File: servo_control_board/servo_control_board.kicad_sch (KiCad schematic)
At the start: 18 parts, among them J1 Conn_01x03_Pin, J2 Conn_01x03_Pin, J3 Conn_01x03_Pin, J4 Conn_01x03_Pin, J5 Conn_01x03_Pin, J6 Conn_01x03_Pin, J7 Conn_01x02_Pin, J8 Conn_01x02_Socket, U1 LTV-846

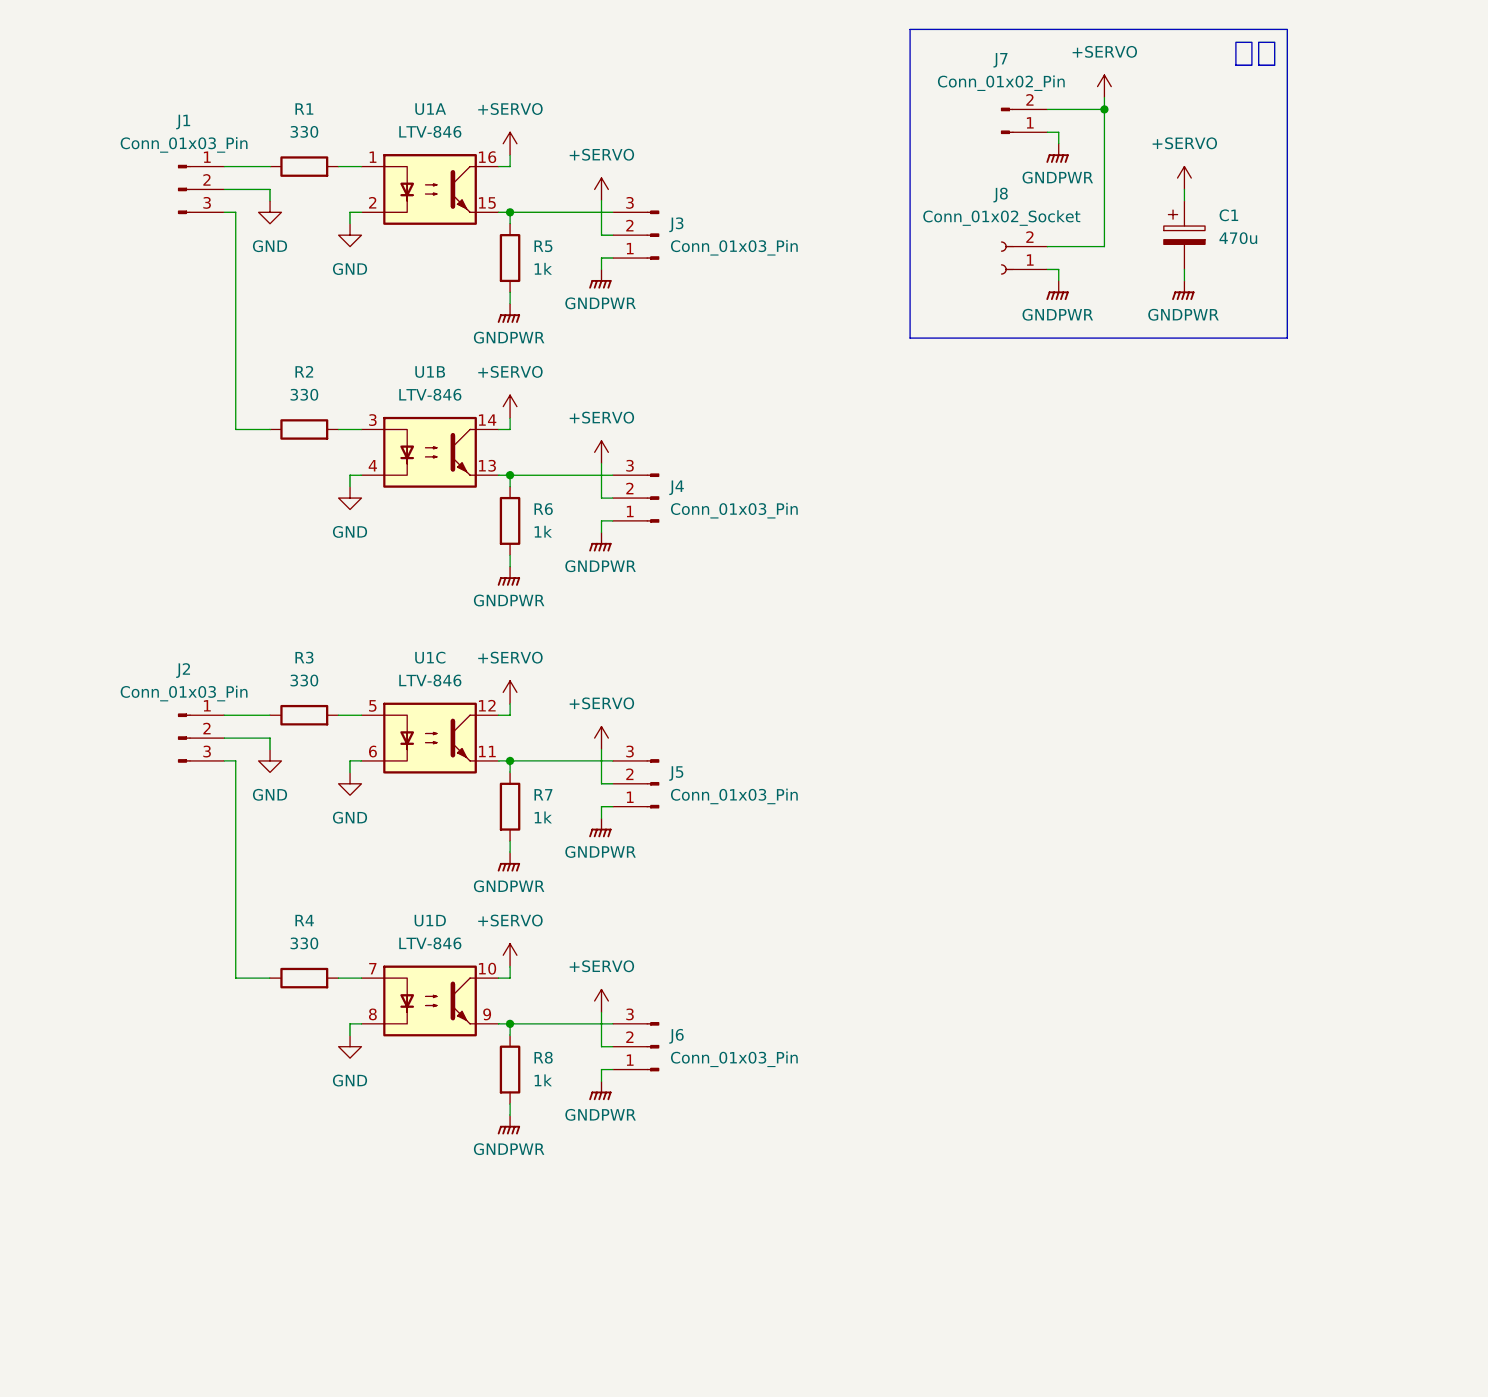
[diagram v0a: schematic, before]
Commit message: サーボ制御基板　使用するフォトカプラを変更 もともと使っていたLTV-846には以下のような問題点があったため． ・応答速度が遅く，サーボの角度にズレが生じる恐れがある ・応答速度を上げようと電流値を上げると，GPIOへの要求電流上昇やCTR不足が生じる
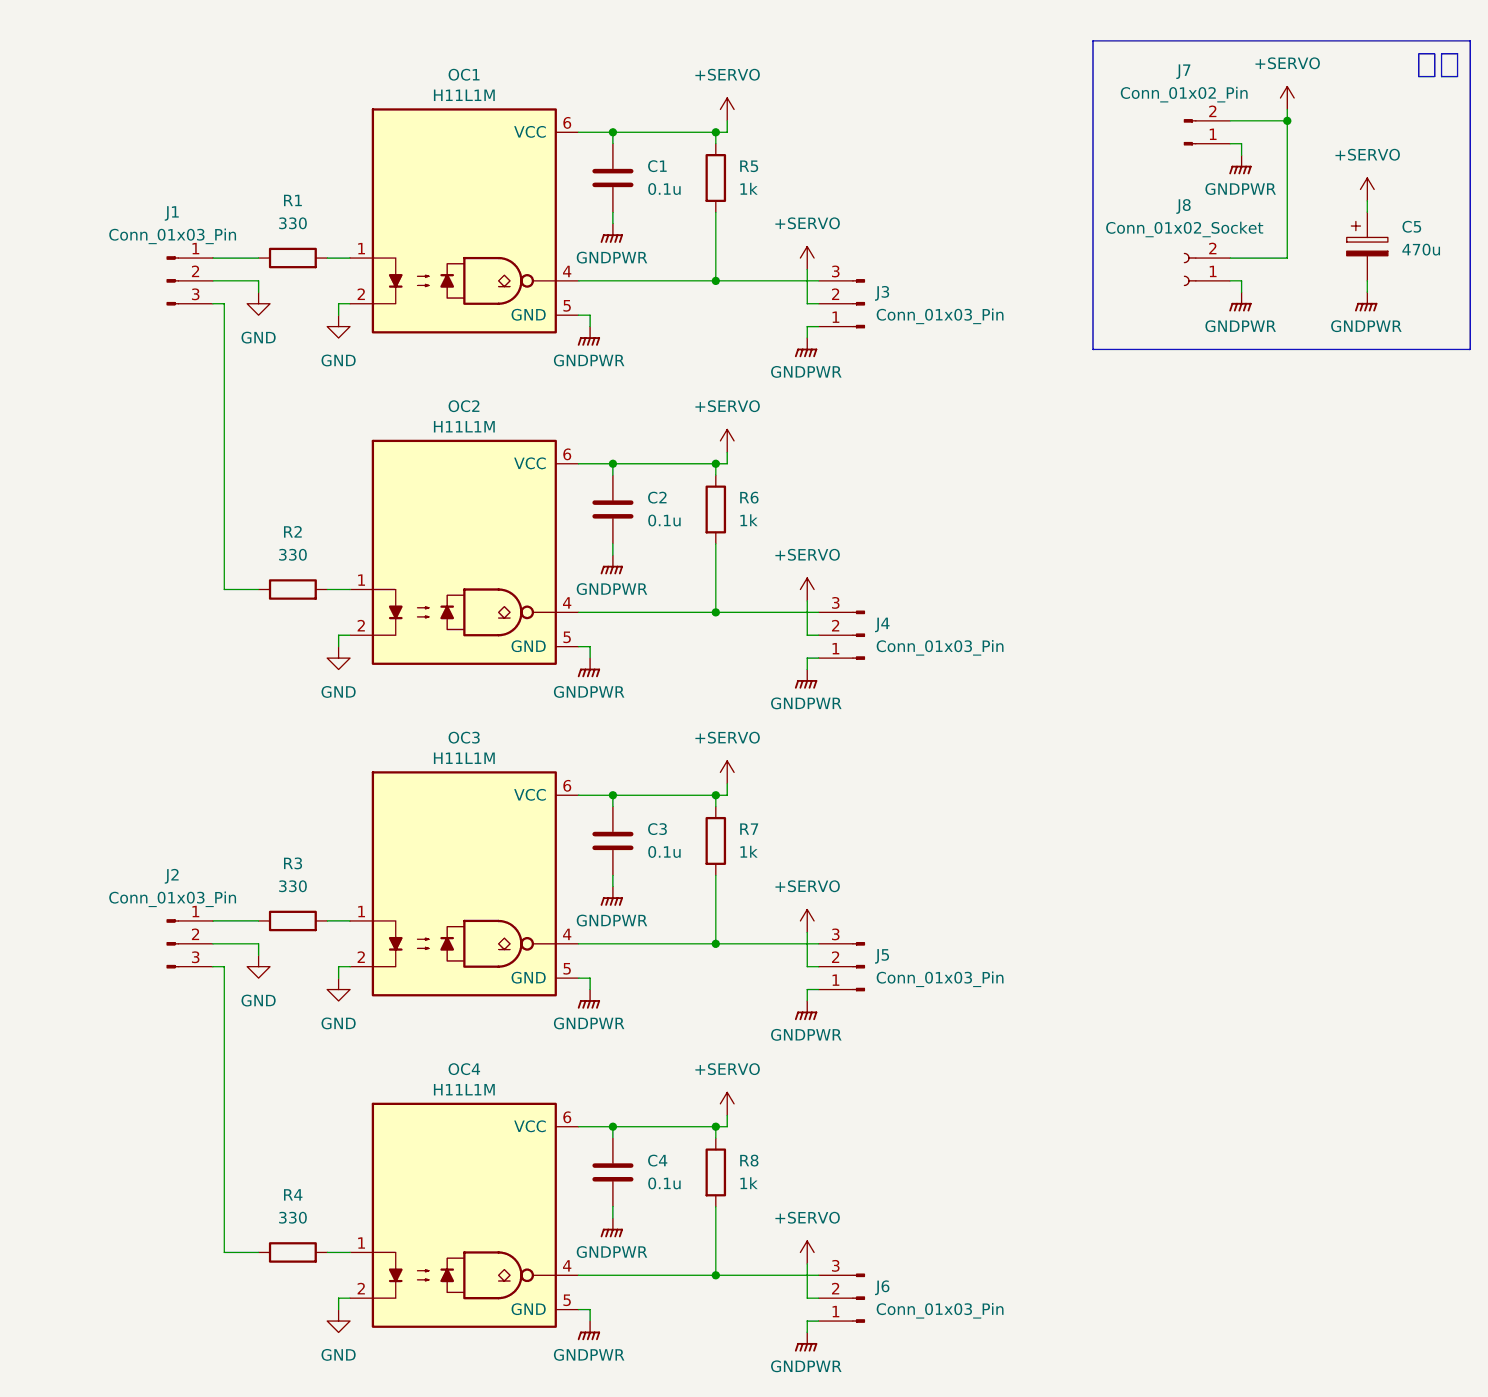
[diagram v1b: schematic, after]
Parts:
- removed U1: LTV-846, Package_DIP:DIP-16_W7.62mm, symbol Isolator:LTV-847
- added C1, C2, C3, C4: 0.1u, PCM_Package_DIP_AKL:DIP-6_W7.62mm_LongPads, symbol Device:C
- added OC1, OC2, OC3, OC4: H11L1M, PCM_Package_DIP_AKL:DIP-6_W7.62mm_LongPads, symbol PCM_Optocoupler_Logic_AKL:H11L1M
- J1, J2: footprint Package_DIP:DIP-16_W7.62mm -> OU_connector:DF1E-3P-2.5DS
- J3, J4, J5, J6: footprint Package_SO:TSSOP-16_4.4x5mm_P0.65mm -> Connector_PinHeader_2.54mm:PinHeader_1x03_P2.54mm_Vertical
- J7: footprint (none) -> OU_connector:AMASS_XT30PW-M_1x02_P2.50mm_Horizontal
- J8: footprint (none) -> OU_connector:AMASS_XT30PW-F_1x02_P2.50mm_Horizontal
- renumbered C1 to C5
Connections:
- net +SERVO: now also R5.1, R6.1, R7.1, R8.1, C1.2, C2.2, C3.2, C4.2, OC1.6 (VCC), OC2.6 (VCC), OC3.6 (VCC), OC4.6 (VCC)
- net GND: now also OC1.2, OC2.2, OC3.2, OC4.2
- net GNDPWR: now also C1.1, C2.1, C3.1, C4.1, OC1.5 (GND), OC2.5 (GND), OC3.5 (GND), OC4.5 (GND); no longer R5.2, R6.2, R7.2, R8.2
- net at J6.3 (Pin_3): now also R8.2, OC4.4; no longer R8.1
- net at J3.3 (Pin_3): now also R5.2, OC1.4; no longer R5.1
- net at J5.3 (Pin_3): now also R7.2, OC3.4; no longer R7.1
- net at R3.2: now also OC3.1
- net at J4.3 (Pin_3): now also R6.2, OC2.4; no longer R6.1
- net at R1.2: now also OC1.1
- net at R4.2: now also OC4.1
- net at R2.2: now also OC2.1
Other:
- moved on the sheet: C5, J1, J2, J3, J7, J8, R1, R2, R3, R4

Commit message: サーボ制御基板　フットプリント割当まで完了
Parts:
- C1, C2, C3, C4: footprint PCM_Package_DIP_AKL:DIP-6_W7.62mm_LongPads -> Capacitor_THT:C_Disc_D5.0mm_W2.5mm_P2.50mm; Buy_URL (none) -> https://akizukidenshi.com/catalog/g/g113582/
- J3, J4, J5, J6: Buy_URL (none) -> https://akizukidenshi.com/catalog/g/g100167/
- J7: Buy_URL (none) -> https://akizukidenshi.com/catalog/g/g117949/
- J8: Buy_URL (none) -> https://akizukidenshi.com/catalog/g/g117948/
- OC1, OC2, OC3, OC4: Buy_URL (none) -> https://akizukidenshi.com/catalog/g/g131184/
- R1, R2, R3, R4: footprint (none) -> Resistor_THT:R_Axial_DIN0207_L6.3mm_D2.5mm_P2.54mm_Vertical; Buy_URL (none) -> https://akizukidenshi.com/catalog/g/g125331/
- R5, R6, R7, R8: footprint (none) -> Resistor_THT:R_Axial_DIN0207_L6.3mm_D2.5mm_P2.54mm_Vertical; Buy_URL (none) -> https://akizukidenshi.com/catalog/g/g125102/

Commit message: サーボ制御基板　ピンヘッダのフットプリントを変更
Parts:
- J3, J4, J5, J6: footprint Connector_PinHeader_2.54mm:PinHeader_1x03_P2.54mm_Vertical -> Connector_PinHeader_2.54mm:PinHeader_1x03_P2.54mm_Horizontal; Buy_URL https://akizukidenshi.com/catalog/g/g100167/ -> https://akizukidenshi.com/catalog/g/g101627/
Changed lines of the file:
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@@
 			)
 		)
-		(property "Footprint" "Connector_PinHeader_2.54mm:PinHeader_1x03_P2.54mm_Vertical"
+		(property "Footprint" "Connector_PinHeader_2.54mm:PinHeader_1x03_P2.54mm_Horizontal"
 			(at 106.68 121.92 0)
 			(hide yes)
@@
 			)
 		)
-		(property "Buy_URL" "https://akizukidenshi.com/catalog/g/g100167/"
+		(property "Buy_URL" "https://akizukidenshi.com/catalog/g/g101627/"
 			(at 106.68 121.92 0)
 			(hide yes)
@@
 			)
 		)
-		(property "Footprint" "Connector_PinHeader_2.54mm:PinHeader_1x03_P2.54mm_Vertical"
+		(property "Footprint" "Connector_PinHeader_2.54mm:PinHeader_1x03_P2.54mm_Horizontal"
 			(at 106.68 85.09 0)
 			(hide yes)
@@
 			)
 		)
-		(property "Buy_URL" "https://akizukidenshi.com/catalog/g/g100167/"
+		(property "Buy_URL" "https://akizukidenshi.com/catalog/g/g101627/"
 			(at 106.68 85.09 0)
 			(hide yes)
@@
 			)
 		)
-		(property "Footprint" "Connector_PinHeader_2.54mm:PinHeader_1x03_P2.54mm_Vertical"
+		(property "Footprint" "Connector_PinHeader_2.54mm:PinHeader_1x03_P2.54mm_Horizontal"
 			(at 106.68 48.26 0)
 			(hide yes)
@@
 			)
 		)
-		(property "Buy_URL" "https://akizukidenshi.com/catalog/g/g100167/"
+		(property "Buy_URL" "https://akizukidenshi.com/catalog/g/g101627/"
 			(at 106.68 48.26 0)
 			(hide yes)
@@
 			)
 		)
-		(property "Footprint" "Connector_PinHeader_2.54mm:PinHeader_1x03_P2.54mm_Vertical"
+		(property "Footprint" "Connector_PinHeader_2.54mm:PinHeader_1x03_P2.54mm_Horizontal"
 			(at 106.68 158.75 0)
 			(hide yes)
@@
 			)
 		)
-		(property "Buy_URL" "https://akizukidenshi.com/catalog/g/g100167/"
+		(property "Buy_URL" "https://akizukidenshi.com/catalog/g/g101627/"
 			(at 106.68 158.75 0)
 			(hide yes)

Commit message: サーボ制御基板　入力端子のピンアサインを変更，電源パススルー出力端子を削除
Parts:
- removed J8: Conn_01x02_Socket, OU_connector:AMASS_XT30PW-F_1x02_P2.50mm_Horizontal, symbol Connector:Conn_01x02_Socket
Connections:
- net at R4.1: now also J2.1 (Pin_1); no longer J2.3 (Pin_3)
- net at R2.1: now also J1.1 (Pin_1); no longer J1.3 (Pin_3)
- net at R3.1: now also J2.3 (Pin_3); no longer J2.1 (Pin_1)
- net at R1.1: now also J1.3 (Pin_3); no longer J1.1 (Pin_1)
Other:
- moved on the sheet: C5, J7

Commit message: サーボ制御基板　入力端子のピンアサインを再度変更
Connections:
- net at R4.1: now also J2.3 (Pin_3); no longer J2.1 (Pin_1)
- net at R2.1: now also J1.3 (Pin_3); no longer J1.1 (Pin_1)
- net at R3.1: now also J2.1 (Pin_1); no longer J2.3 (Pin_3)
- net at R1.1: now also J1.1 (Pin_1); no longer J1.3 (Pin_3)
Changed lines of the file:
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@@
 		(dnp no)
 		(fields_autoplaced yes)
-		(property "Reference" "#PWR027"
+		(property "Reference" "#PWR028"
 			(at 152.4 44.45 0)
 			(hide yes)
@@
 			(project "servo_control_board"
 				(path "/513b22f8-6087-410c-ac00-1a70f49ac862"
-					(reference "#PWR027")
+					(reference "#PWR028")
 					(unit 1)
 				)
@@
 		(lib_id "Connector:Conn_01x03_Pin")
 		(at 29.21 119.38 0)
-		(mirror x)
 		(unit 1)
 		(body_style 1)
@@
 		(dnp no)
 		(property "Reference" "J2"
-			(at 29.21 110.744 0)
+			(at 29.21 110.49 0)
 			(show_name no)
 			(do_not_autoplace no)
@@
 		)
 		(property "Value" "Conn_01x03_Pin"
-			(at 29.21 113.538 0)
+			(at 29.21 113.284 0)
 			(show_name no)
 			(do_not_autoplace no)
@@
 		(lib_id "Connector:Conn_01x03_Pin")
 		(at 29.21 45.72 0)
-		(mirror x)
 		(unit 1)
 		(body_style 1)
@@
 		(dnp no)
 		(property "Reference" "J1"
-			(at 29.21 37.084 0)
+			(at 29.21 36.83 0)
 			(show_name no)
 			(do_not_autoplace no)
@@
 		)
 		(property "Value" "Conn_01x03_Pin"
-			(at 29.21 39.878 0)
+			(at 29.21 39.624 0)
 			(show_name no)
 			(do_not_autoplace no)
@@
 		(dnp no)
 		(fields_autoplaced yes)
-		(property "Reference" "#PWR029"
+		(property "Reference" "#PWR027"
 			(at 152.4 30.48 0)
 			(hide yes)
@@
 			(project "servo_control_board"
 				(path "/513b22f8-6087-410c-ac00-1a70f49ac862"
-					(reference "#PWR029")
-					(unit 1)
-				)
+					(reference "#PWR027")
+					(unit 1)
+				)

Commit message: サーボ制御基板　基板完成，ver0.1
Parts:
- added TP1, TP2, TP4, TP5, TP6, TP7, TP8, TP9: TestPoint_Probe, TestPoint:TestPoint_THTPad_D2.0mm_Drill1.0mm, symbol Connector:TestPoint_Probe
- added TP10, TP3: TestPoint, TestPoint:TestPoint_THTPad_D2.0mm_Drill1.0mm, symbol Connector:TestPoint
- renumbered R2 to R1, R4 to R2, R1 to R3, R3 to R4, OC1 to U1, OC2 to U2, OC3 to U3, OC4 to U4
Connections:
- net GND: now also TP3.1
- net GNDPWR: now also TP10.1
- net at J5.3 (Pin_3), R7.2, U3.4: now also TP8.1
- net at J4.3 (Pin_3), R6.2, U2.4: now also TP7.1
- net at J3.3 (Pin_3), R5.2, U1.4: now also TP6.1
- net at J2.3 (Pin_3), R2.1: now also TP2.1
- net at J1.3 (Pin_3), R1.1: now also TP1.1
- net at J2.1 (Pin_1), R4.1: now also TP5.1
- net at J1.1 (Pin_1), R3.1: now also TP4.1
- net at J6.3 (Pin_3), R8.2, U4.4: now also TP9.1
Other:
- moved on the sheet: J1, J2, R3, R4

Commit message: サーボ制御基板　コネクタをJST PAに変更
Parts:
- J1, J2: footprint OU_connector:DF1E-3P-2.5DS -> OU_connector:S03B-PASK-2
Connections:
- net at R3.1, TP4.1: now also J1.3 (Pin_3); no longer J1.1 (Pin_1)
- net at R2.1, TP2.1: now also J2.1 (Pin_1); no longer J2.3 (Pin_3)
- net at R1.1, TP1.1: now also J1.1 (Pin_1); no longer J1.3 (Pin_3)
- net at R4.1, TP5.1: now also J2.3 (Pin_3); no longer J2.1 (Pin_1)
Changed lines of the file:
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@@
 		(lib_id "Connector:Conn_01x03_Pin")
 		(at 21.59 119.38 0)
+		(mirror x)
 		(unit 1)
 		(body_style 1)
@@
 		(dnp no)
 		(property "Reference" "J2"
-			(at 21.59 110.49 0)
+			(at 21.59 110.998 0)
 			(show_name no)
 			(do_not_autoplace no)
@@
 		)
 		(property "Value" "Conn_01x03_Pin"
-			(at 21.59 113.284 0)
-			(show_name no)
-			(do_not_autoplace no)
-			(effects
-				(font
-					(size 1.27 1.27)
-				)
-			)
-		)
-		(property "Footprint" "OU_connector:DF1E-3P-2.5DS"
+			(at 21.59 113.538 0)
+			(show_name no)
+			(do_not_autoplace no)
+			(effects
+				(font
+					(size 1.27 1.27)
+				)
+			)
+		)
+		(property "Footprint" "OU_connector:S03B-PASK-2"
 			(at 21.59 119.38 0)
 			(hide yes)
@@
 			)
 		)
-		(property "Description" "DF1E-3P-2.5DS"
+		(property "Description" "S03B-PASK-2"
 			(at 21.59 119.38 0)
 			(hide yes)
@@
 		(lib_id "Connector:Conn_01x03_Pin")
 		(at 21.59 45.72 0)
+		(mirror x)
 		(unit 1)
 		(body_style 1)
@@
 		(dnp no)
 		(property "Reference" "J1"
-			(at 21.59 36.83 0)
+			(at 21.59 37.592 0)
 			(show_name no)
 			(do_not_autoplace no)
@@
 		)
 		(property "Value" "Conn_01x03_Pin"
-			(at 21.59 39.624 0)
-			(show_name no)
-			(do_not_autoplace no)
-			(effects
-				(font
-					(size 1.27 1.27)
-				)
-			)
-		)
-		(property "Footprint" "OU_connector:DF1E-3P-2.5DS"
+			(at 21.59 39.878 0)
+			(show_name no)
+			(do_not_autoplace no)
+			(effects
+				(font
+					(size 1.27 1.27)
+				)
+			)
+		)
+		(property "Footprint" "OU_connector:S03B-PASK-2"
 			(at 21.59 45.72 0)
 			(hide yes)
@@
 			)
 		)
-		(property "Description" "DF1E-3P-2.5DS"
+		(property "Description" "S03B-PASK-2"
 			(at 21.59 45.72 0)
 			(hide yes)
